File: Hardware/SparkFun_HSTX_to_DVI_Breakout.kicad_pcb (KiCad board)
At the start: 4 copper layers, 25.4 x 25.4 mm, 30 parts, among them J1 Conn_01x22_FPC_0.5mm_RA, J2 HDMI, Q1 BSS138, U1 AP3602

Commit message: Update SparkFun_HSTX_to_DVI_Breakout.kicad_pcb
Add Impedance control to Ordering instructions
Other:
- board text added: "Impedance: JLC7628"
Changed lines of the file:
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@@
 		(tags "SparkFun resistor")
 		(property "Reference" "R4"
-			(at 0 -1.17 360)
+			(at 0 -1.17 0)
 			(layer "F.Fab")
 			(effects
@@
 		)
 		(property "Value" "100k"
-			(at 0 1.17 360)
+			(at 0 1.17 0)
 			(layer "F.Fab")
 			(effects
@@
 				(font
 					(size 0.001 0.001)
+					(thickness 0.15)
 				)
 			)
@@
 				(font
 					(size 0.001 0.001)
+					(thickness 0.15)
 				)
 			)
@@
 				(font
 					(size 0.001 0.001)
+					(thickness 0.15)
 				)
 			)
@@
 				(font
 					(size 0.001 0.001)
+					(thickness 0.15)
 				)
 			)
@@
 		(tags "SparkFun capacitor")
 		(property "Reference" "C2"
-			(at 0 -1.43 360)
+			(at 0 -1.43 0)
 			(layer "F.Fab")
 			(effects
@@
 		)
 		(property "Value" "1.0uF"
-			(at 0 1.43 360)
+			(at 0 1.43 0)
 			(layer "F.Fab")
 			(effects
@@
 		(tags "SparkFun resistor")
 		(property "Reference" "R5"
-			(at 0 -1.17 360)
+			(at 0 -1.17 0)
 			(layer "F.Fab")
 			(effects
@@
 		)
 		(property "Value" "100k"
-			(at 0 1.17 360)
+			(at 0 1.17 0)
 			(layer "F.Fab")
 			(effects
@@
 		(fp_arc
 			(start 0.762 -1.016)
-			(mid 1.08529 -0.88209)
+			(mid 1.085289 -0.882089)
 			(end 1.2192 -0.5588)
 			(stroke
@@
 				(font
 					(size 0.001 0.001)
+					(thickness 0.15)
 				)
 				(justify mirror)
@@
 				(font
 					(size 0.001 0.001)
+					(thickness 0.15)
 				)
 				(justify mirror)
@@
 				(font
 					(size 0.001 0.001)
+					(thickness 0.15)
 				)
 				(justify mirror)
@@
 				(font
 					(size 0.001 0.001)
+					(thickness 0.15)
 				)
 				(justify mirror)
@@
 				(font
 					(size 0.001 0.001)
+					(thickness 0.15)
 				)
 				(justify mirror)
@@
 				(font
 					(size 0.001 0.001)
+					(thickness 0.15)
 				)
 				(justify mirror)
@@
 		(fp_arc
 			(start 0.762 -1.016)
-			(mid 1.08529 -0.88209)
+			(mid 1.085289 -0.882089)
 			(end 1.2192 -0.5588)
 			(stroke
@@
 				(font
 					(size 0.001 0.001)
+					(thickness 0.15)
 				)
 				(justify mirror)
@@
 				(font
 					(size 0.001 0.001)
+					(thickness 0.15)
 				)
 				(justify mirror)
@@
 		(layer "Eco1.User")
 		(effects
+			(font
+				(size 1.27 1.27)
+				(thickness 0.15)
+			)
+			(justify left bottom)
+		)
+	)
+	(gr_text "Impedance: JLC7628"
+		(at 245.8 171.6 0)
+		(layer "Eco1.User")
+		(effects

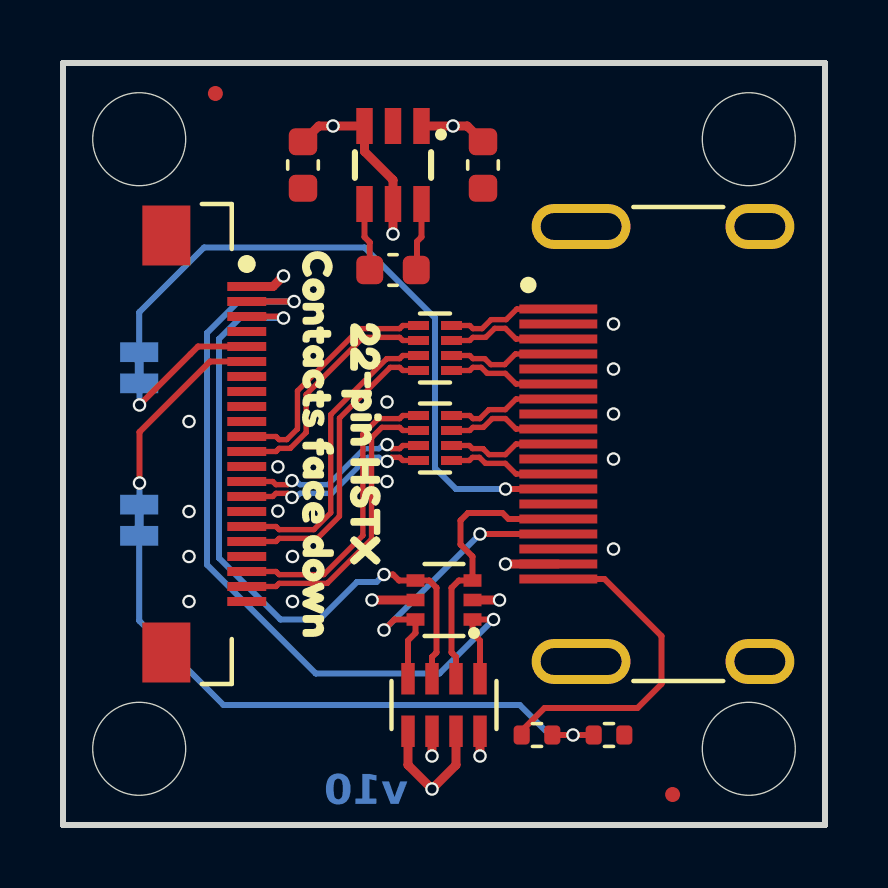
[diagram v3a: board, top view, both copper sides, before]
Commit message: Design review updates
Fix wandering measure.
Move 5V trace to avoid splitting 3.3V vias.
Add more ground vias.
Delete unused README.
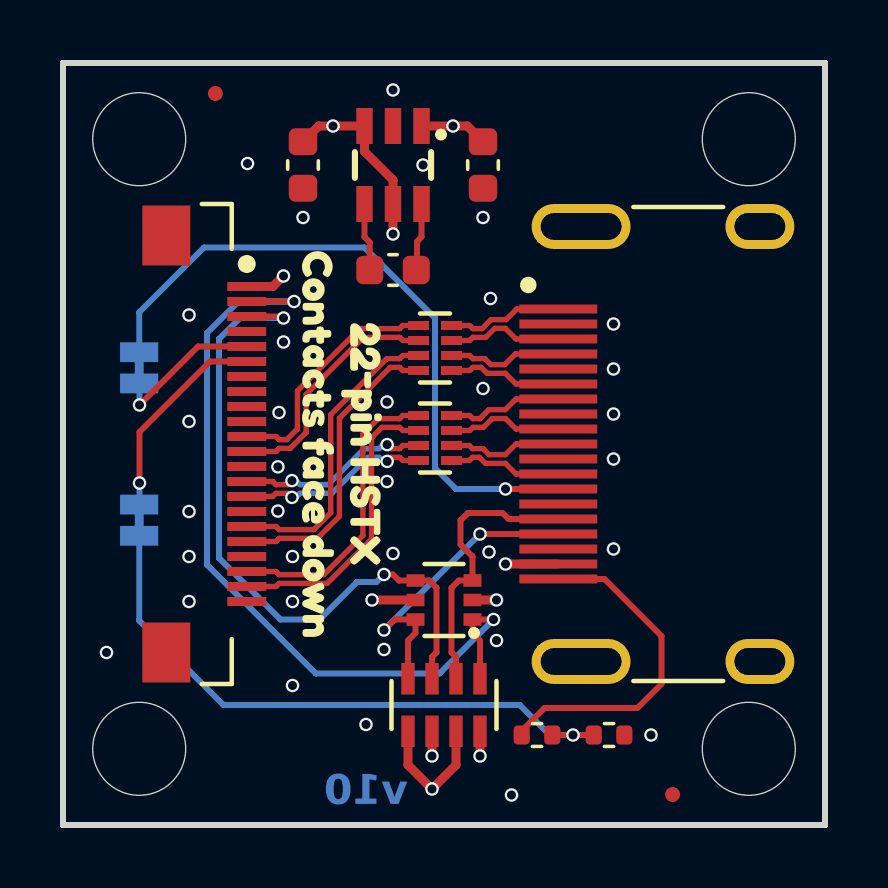
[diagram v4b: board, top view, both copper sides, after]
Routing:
- net 5V: track 33.9 -> 34.5 mm
- net GND: vias 15 -> 34
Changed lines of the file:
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@@
 			(remove_unused_layers yes)
 			(keep_end_layers yes)
-			(zone_layer_connections)
+			(zone_layer_connections "In1.Cu")
 			(net 1 "GND")
 			(pinfunction "SH")
@@
 			(remove_unused_layers yes)
 			(keep_end_layers yes)
-			(zone_layer_connections)
+			(zone_layer_connections "In1.Cu")
 			(net 1 "GND")
 			(pinfunction "SH")
@@
 			(remove_unused_layers yes)
 			(keep_end_layers yes)
-			(zone_layer_connections)
+			(zone_layer_connections "In1.Cu")
 			(net 1 "GND")
 			(pinfunction "SH")
@@
 			(remove_unused_layers yes)
 			(keep_end_layers yes)
-			(zone_layer_connections)
+			(zone_layer_connections "In1.Cu")
 			(net 1 "GND")
 			(pinfunction "SH")
@@
 		(height -5.08)
 		(orientation 1)
-		(gr_text "12.7 mm"
+		(gr_text "0.5 in"
 			(at 93.42 138.15 90)
 			(layer "Dwgs.User")
@@
 		(layer "Dwgs.User")
 		(pts
-			(xy 98.5 144.5) (xy 126.44 144.5)
+			(xy 98.5 144.5) (xy 126.44 139.05)
 		)
 		(height 8.382)
 		(orientation 0)
-		(gr_text "27.94 mm"
+		(gr_text "1.1 in"
 			(at 112.47 152.882 0)
 			(layer "Dwgs.User")
@@
 		(height 6.1)
 		(orientation 0)
-		(gr_text "25.4 mm"
+		(gr_text "1 in"
 			(at 111.2 150.6 0)
 			(layer "Dwgs.User")
@@
 		(height 2.3)
 		(orientation 0)
-		(gr_text "2.54 mm"
+		(gr_text "0.1 in"
 			(at 103.58 146.8 0)
 			(layer "Dwgs.User")
@@
 		(height -10.16)
 		(orientation 1)
-		(gr_text "25.4 mm"
+		(gr_text "1 in"
 			(at 88.34 131.8 90)
 			(layer "Dwgs.User")
@@
 		(height -7.62)
 		(orientation 1)
-		(gr_text "22.86 mm"
+		(gr_text "0.9 in"
 			(at 90.88 133.07 90)
 			(layer "Dwgs.User")
@@
 		(height -2.54)
 		(orientation 1)
-		(gr_text "2.54 mm"
+		(gr_text "0.1 in"
 			(at 95.96 139.166 90)
 			(layer "Dwgs.User")
@@
 		(height 3.9)
 		(orientation 0)
-		(gr_text "22.86 mm"
+		(gr_text "0.9 in"
 			(at 109.93 148.4 0)
 			(layer "Dwgs.User")
@@
 	)
 	(via
+		(at 112.5 124.25)
+		(size 0.45)
+		(drill 0.3)
+		(layers "F.Cu" "B.Cu")
+		(free yes)
+		(net 1)
+	)
+	(via
 		(at 105.663878 132.561024)
 		(size 0.45)
@@
 	)
 	(via
+		(at 110.5 122.5)
+		(size 0.45)
+		(drill 0.3)
+		(layers "F.Cu" "B.Cu")
+		(free yes)
+		(net 1)
+	)
+	(via
+		(at 109.2 138.65)
+		(size 0.45)
+		(drill 0.3)
+		(layers "F.Cu" "B.Cu")
+		(free yes)
+		(net 1)
+	)
+	(via
 		(at 102.7 134.05)
 		(size 0.45)
@@
 	)
 	(via
+		(at 104.65 122.45)
+		(size 0.45)
+		(drill 0.3)
+		(layers "F.Cu" "B.Cu")
+		(free yes)
+		(net 1)
+	)
+	(via
+		(at 105.85 128.4)
+		(size 0.45)
+		(drill 0.3)
+		(layers "F.Cu" "B.Cu")
+		(free yes)
+		(net 1)
+	)
+	(via
+		(at 105.7 130.75)
+		(size 0.45)
+		(drill 0.3)
+		(layers "F.Cu" "B.Cu")
+		(free yes)
+		(net 1)
+	)
+	(via
+		(at 99.95 138.75)
+		(size 0.45)
+		(drill 0.3)
+		(layers "F.Cu" "B.Cu")
+		(free yes)
+		(net 1)
+	)
+	(via
+		(at 106.15 139.85)
+		(size 0.45)
+		(drill 0.3)
+		(layers "F.Cu" "B.Cu")
+		(free yes)
+		(net 1)
+	)
+	(via
 		(at 106.15 137.05)
 		(size 0.45)
@@
 	)
 	(via
+		(at 102.7 127.5)
+		(size 0.45)
+		(drill 0.3)
+		(layers "F.Cu" "B.Cu")
+		(free yes)
+		(net 1)
+	)
+	(via
+		(at 106.5 124.25)
+		(size 0.45)
+		(drill 0.3)
+		(layers "F.Cu" "B.Cu")
+		(free yes)
+		(net 1)
+	)
+	(via
+		(at 112.7 135.4)
+		(size 0.45)
+		(drill 0.3)
+		(layers "F.Cu" "B.Cu")
+		(free yes)
+		(net 1)
+	)
+	(via
+		(at 113.45 143.5)
+		(size 0.45)
+		(drill 0.3)
+		(layers "F.Cu" "B.Cu")
+		(free yes)
+		(net 1)
+	)
+	(via
 		(at 109.3 133.05)
 		(size 0.45)
@@
 	)
 	(via
+		(at 112.95 138.35)
+		(size 0.45)
+		(drill 0.3)
+		(layers "F.Cu" "B.Cu")
+		(free yes)
+		(net 1)
+	)
+	(via
 		(at 116.85 127.8)
 		(size 0.45)
@@
 	)
 	(via
+		(at 109.5 135.45)
+		(size 0.45)
+		(drill 0.3)
+		(layers "F.Cu" "B.Cu")
+		(free yes)
+		(net 1)
+	)
+	(via
+		(at 112.75 126.95)
+		(size 0.45)
+		(drill 0.3)
+		(layers "F.Cu" "B.Cu")
+		(free yes)
+		(net 1)
+	)
+	(via
 		(at 116.85 130.8)
 		(size 0.45)
@@
 	)
 	(via
+		(at 108.6 141.15)
+		(size 0.45)
+		(drill 0.3)
+		(layers "F.Cu" "B.Cu")
+		(free yes)
+		(net 1)
+	)
+	(via
 		(at 102.7 131.05)
 		(size 0.45)
@@
 	)
 	(via
-		(at 116.85 132.3)
+		(at 118.1 141.5)
 		(size 0.45)
 		(drill 0.3)
@@
 		(net 1)
 	)
-	(segment
-		(start 112.15 137)
-		(end 113.05 137)
-		(width 0.3)
-		(layer "F.Cu")
-		(net 2)
+	(via
+		(at 112.5 129.95)
+		(size 0.45)
+		(drill 0.3)
+		(layers "F.Cu" "B.Cu")
+		(free yes)
+		(net 1)
+	)
+	(via
+		(at 109.5 120)
+		(size 0.45)
+		(drill 0.3)
+		(layers "F.Cu" "B.Cu")
+		(free yes)
+		(net 1)
+	)
+	(via
+		(at 116.85 132.3)
+		(size 0.45)
+		(drill 0.3)
+		(layers "F.Cu" "B.Cu")
+		(free yes)
+		(net 1)
 	)
 	(segment
@@
 		(net 2)
 	)
+	(segment
+		(start 112.15 137)
+		(end 112.95 137)
+		(width 0.3)
+		(layer "F.Cu")
+		(net 2)
+	)
 	(via
-		(at 113.05 137)
+		(at 112.95 137)
 		(size 0.45)
 		(drill 0.3)
@@
 	)
 	(segment
-		(start 114.25 134.8)
-		(end 114.25 127.15)
+		(start 113.6 142.2)
+		(end 113.6 136.55)
 		(width 0.3)
 		(layer "In2.Cu")
@@
 	)
 	(segment
-		(start 110 139.05)
-		(end 113.25 135.8)
+		(start 113.6 136.55)
+		(end 113.25 136.2)
 		(width 0.3)
 		(layer "In2.Cu")
@@
 	)
 	(segment
-		(start 111.5 124.4)
-		(end 111.5 121.2)
+		(start 112.5 143.3)
+		(end 113.6 142.2)
 		(width 0.3)
 		(layer "In2.Cu")
@@
 	)
 	(segment
-		(start 110.8 143.3)
-		(end 110 142.5)
+		(start 114.25 134.8)
+		(end 114.25 127.15)
 		(width 0.3)
 		(layer "In2.Cu")
@@
 	)
 	(segment
-		(start 110 142.5)
-		(end 110 139.05)
+		(start 111.5 124.4)
+		(end 111.5 121.2)
+		(width 0.3)
+		(layer "In2.Cu")
+		(net 5)
+	)
+	(segment
+		(start 110.8 143.3)
+		(end 112.5 143.3)
 		(width 0.3)
 		(layer "In2.Cu")
@@
 		(width 0.3)
 		(layer "In2.Cu")
+		(net 5)
+	)
+	(segment
+		(start 113.25 136.2)
+		(end 113.25 135.8)
+		(width 0.3)
+		(layer "In2.Cu")
